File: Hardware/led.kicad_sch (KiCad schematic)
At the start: 23 parts, among them U5 TLC59208FIPWR

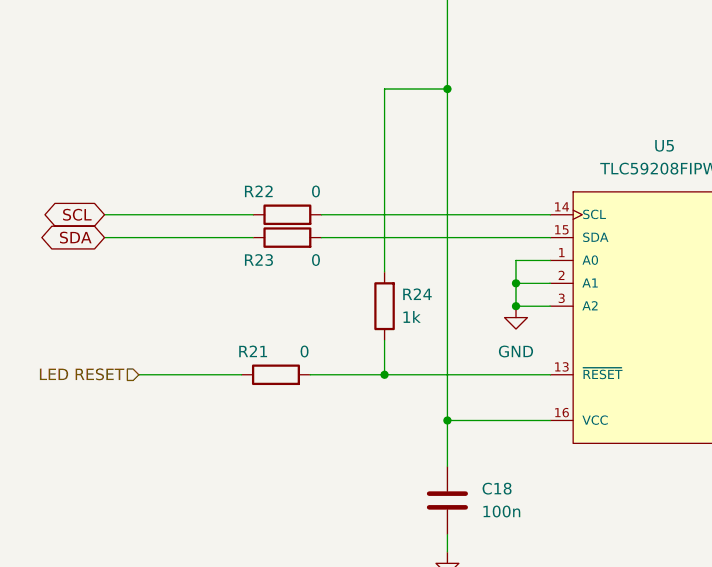
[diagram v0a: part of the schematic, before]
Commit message: removed 2.5v circuit to use the built in variable ldo on the ADC added ~4.915Mhz crystal for 50/60Hz filtering fixed several small schematic issues completely relaid out the board.
Signed-off-by: lokimetasmith <lokimail@gmail.com>
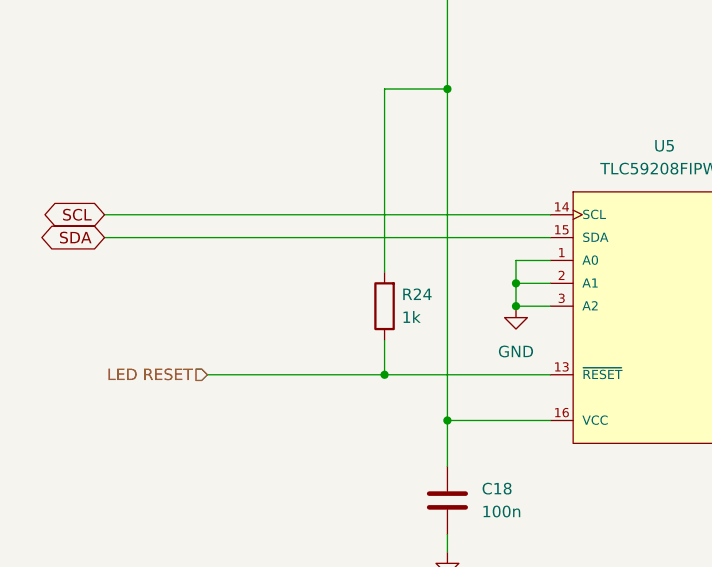
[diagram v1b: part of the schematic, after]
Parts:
- removed R21, R22, R23: 0, Resistor_SMD:R_0603_1608Metric_Pad0.98x0.95mm_HandSolder, symbol Device:R
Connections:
- net LED RESET: now also R24.1, U5.13 (~{RESET})
- net SCL: now also U5.14 (SCL)
- net SDA: now also U5.15 (SDA)
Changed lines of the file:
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@@
     (stroke (width 0) (type default) (color 0 0 0 0))
   )
-  (wire (pts (xy 109.22 95.25) (xy 134.62 95.25))
+  (wire (pts (xy 85.09 95.25) (xy 134.62 95.25))
     (stroke (width 0) (type default) (color 0 0 0 0))
   )
@@
     (stroke (width 0) (type default) (color 0 0 0 0))
   )
-  (wire (pts (xy 109.22 92.71) (xy 134.62 92.71))
+  (wire (pts (xy 85.09 92.71) (xy 134.62 92.71))
     (stroke (width 0) (type default) (color 0 0 0 0))
   )
@@
     (stroke (width 0) (type default) (color 0 0 0 0))
   )
-  (wire (pts (xy 107.95 110.49) (xy 116.205 110.49))
-    (stroke (width 0) (type default) (color 0 0 0 0))
-  )
-  (wire (pts (xy 85.09 95.25) (xy 101.6 95.25))
+  (wire (pts (xy 96.52 110.49) (xy 116.205 110.49))
     (stroke (width 0) (type default) (color 0 0 0 0))
   )
@@
     (stroke (width 0) (type default) (color 0 0 0 0))
   )
-  (wire (pts (xy 85.09 92.71) (xy 101.6 92.71))
-    (stroke (width 0) (type default) (color 0 0 0 0))
-  )
   (wire (pts (xy 160.02 100.33) (xy 173.99 100.33))
     (stroke (width 0) (type default) (color 0 0 0 0))
@@
   )
   (wire (pts (xy 130.81 97.79) (xy 130.81 100.33))
-    (stroke (width 0) (type default) (color 0 0 0 0))
-  )
-  (wire (pts (xy 88.9 110.49) (xy 100.33 110.49))
     (stroke (width 0) (type default) (color 0 0 0 0))
   )
@@
     )
   )
-  (hierarchical_label "LED RESET" (shape input) (at 88.9 110.49 180)
+  (hierarchical_label "LED RESET" (shape input) (at 96.52 110.49 180)
     (effects (font (size 1.27 1.27)) (justify right))
-  )
-  (symbol (lib_id "Device:R") (at 105.41 95.25 90) (unit 1)
-    (in_bom yes) (on_board yes)
-    (property "Reference" "R23" (id 0) (at 102.235 97.79 90))
-    (property "Value" "0" (id 1) (at 108.585 97.79 90))
-    (property "Footprint" "Resistor_SMD:R_0603_1608Metric_Pad0.98x0.95mm_HandSolder" (id 2) (at 105.41 97.028 90)
-      (effects (font (size 1.27 1.27)) hide)
-    )
-    (property "Datasheet" "~" (id 3) (at 105.41 95.25 0)
-      (effects (font (size 1.27 1.27)) hide)
-    )
-    (pin "1")
-    (pin "2")
   )
   (symbol (lib_id "Device:LED") (at 201.93 100.33 0) (unit 1)
@@
     (pin "1")
   )
-  (symbol (lib_id "Device:R") (at 104.14 110.49 90) (unit 1)
-    (in_bom yes) (on_board yes)
-    (property "Reference" "R21" (id 0) (at 101.6 107.95 90))
-    (property "Value" "0" (id 1) (at 107.315 107.95 90))
-    (property "Footprint" "Resistor_SMD:R_0603_1608Metric_Pad0.98x0.95mm_HandSolder" (id 2) (at 104.14 112.268 90)
-      (effects (font (size 1.27 1.27)) hide)
-    )
-    (property "Datasheet" "~" (id 3) (at 104.14 110.49 0)
-      (effects (font (size 1.27 1.27)) hide)
-    )
-    (pin "1")
-    (pin "2")
-  )
   (symbol (lib_id "Device:R") (at 116.205 102.87 180) (unit 1)
     (in_bom yes) (on_board yes) (fields_autoplaced)
@@
       (effects (font (size 1.27 1.27)) hide)
     )
-    (pin "1")
-    (pin "2")
-  )
-  (symbol (lib_id "Device:R") (at 105.41 92.71 90) (unit 1)
-    (in_bom yes) (on_board yes)
-    (property "Reference" "R22" (id 0) (at 102.235 90.17 90))
-    (property "Value" "0" (id 1) (at 108.585 90.17 90))
-    (property "Footprint" "Resistor_SMD:R_0603_1608Metric_Pad0.98x0.95mm_HandSolder" (id 2) (at 105.41 94.488 90)
-      (effects (font (size 1.27 1.27)) hide)
-    )
-    (property "Datasheet" "~" (id 3) (at 105.41 92.71 0)
-      (effects (font (size 1.27 1.27)) hide)
-    )

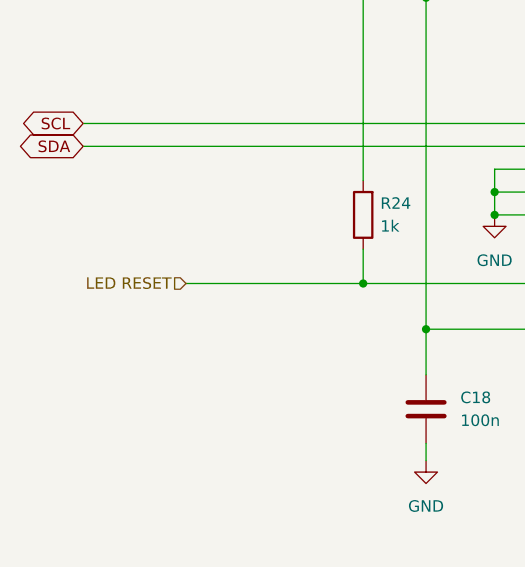
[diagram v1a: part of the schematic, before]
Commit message: in the absence of design docs, I just did my own thing.  I've kept the ribbon cable, but I am not sure why there are one on either side, I've also brought out most of the interrupt lines on the through hole headers, the headers are designed for placement on a carrier board, negating the need for the ribbon cable when the board is stacked
Signed-off-by: lokimetasmith <lokimail@gmail.com>
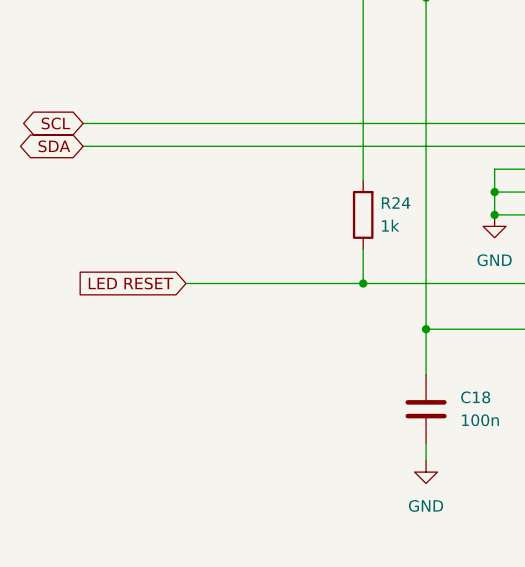
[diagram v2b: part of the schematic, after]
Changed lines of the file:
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@@
+    )
+  )
+  (global_label "LED RESET" (shape input) (at 96.52 110.49 180) (fields_autoplaced)
+    (effects (font (size 1.27 1.27)) (justify right))
+    (property "Intersheet References" "${INTERSHEET_REFS}" (id 0) (at 83.9469 110.4106 0)
+      (effects (font (size 1.27 1.27)) (justify right) hide)
     )
   )
@@
     )
   )
-  (hierarchical_label "LED RESET" (shape input) (at 96.52 110.49 180)
-    (effects (font (size 1.27 1.27)) (justify right))
-  )
   (symbol (lib_id "Device:LED") (at 201.93 100.33 0) (unit 1)
